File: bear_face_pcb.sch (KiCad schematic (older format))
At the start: 201 parts, among them J1 GT-USB-7010EN, J2 Conn_02x03_Odd_Even, SW1 RESET, U1 ATmega32U4-AU, U2 SRV05-4, Y1 16MHz

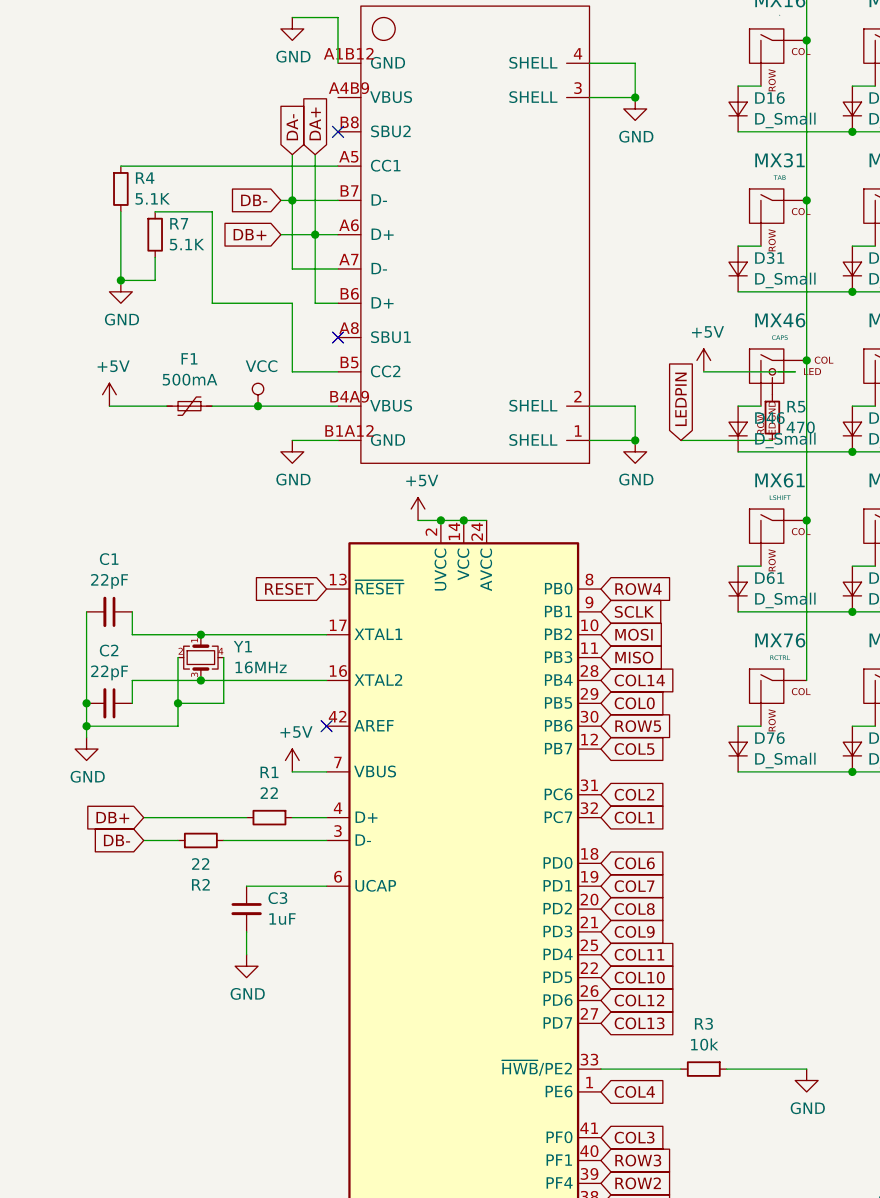
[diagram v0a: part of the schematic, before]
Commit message: renumbered pulldown resistors
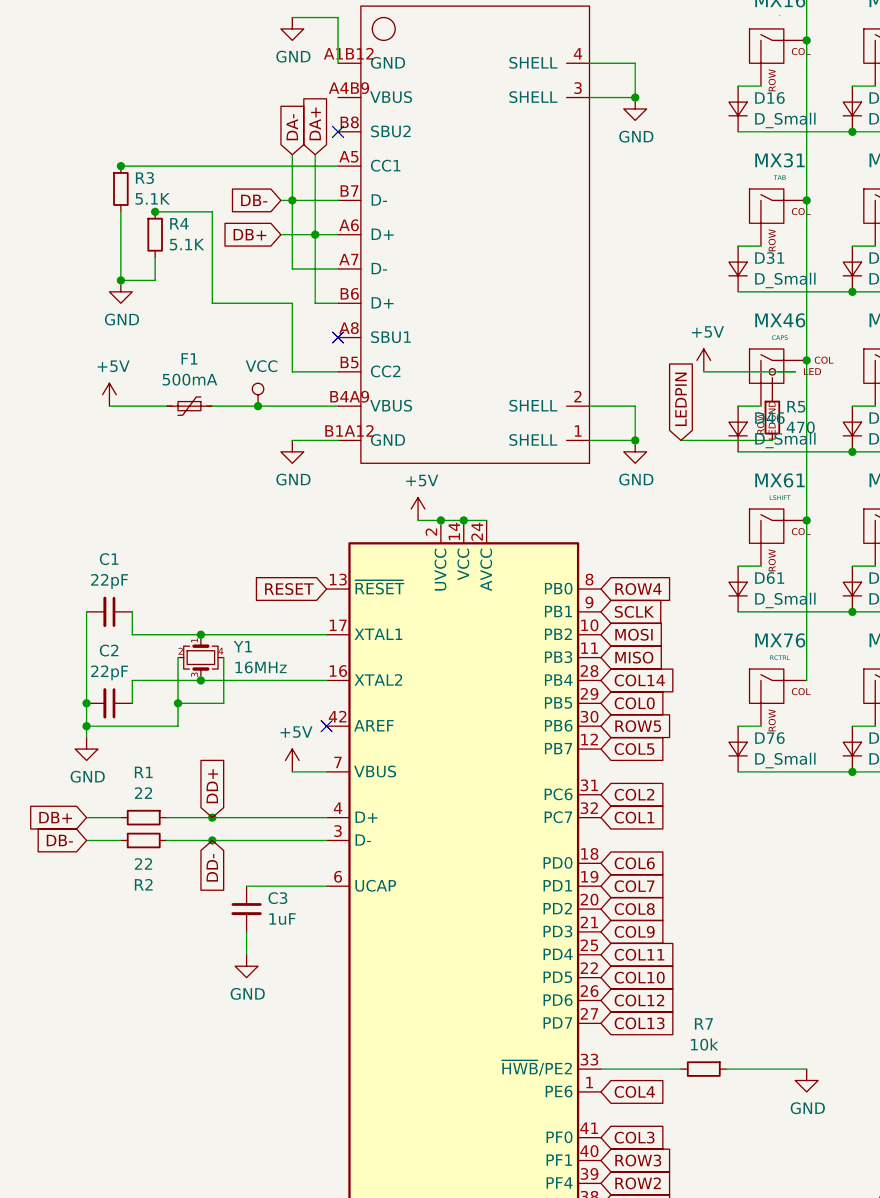
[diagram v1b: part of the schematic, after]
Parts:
- renumbered R4 to R3, R7 to R4, R3 to R7
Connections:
- net DD-: now reaches R2.2, U1.3 (D-)
- net DD+: now reaches R1.1, U1.4 (D+)
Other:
- moved on the sheet: R1, R2
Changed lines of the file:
@@
 	8500 5550 8500 5650
 $Comp
-L Device:R_Small R3
+L Device:R_Small R7
 U 1 1 5E285AAF
 P 3400 6250
-F 0 "R3" V 3204 6250 50  0000 C CNN
+F 0 "R7" V 3204 6250 50  0000 C CNN
 F 1 "10k" V 3295 6250 50  0000 C CNN
 F 2 "Resistor_SMD:R_0805_2012Metric" H 3400 6250 50  0001 C CNN
@@
 Text GLabel 5500 5900 2    50   Input ~ 0
 DA+
-Text GLabel 1550 2450 0    50   Input ~ 0
-DB-
 Text GLabel 3300 3500 1    50   Input ~ 0
 LEDPIN
-Text GLabel 950  5150 0    50   Input ~ 0
-DB+
-Text GLabel 950  5250 0    50   Input ~ 0
-DB-
 Wire Wire Line
 	2250 7450 2350 7450
@@
 Wire Wire Line
 	1700 2600 1550 2600
-Text GLabel 1550 2600 0    50   Input ~ 0
-DB+
 Wire Wire Line
 	1700 2250 1700 2600
@@
 	1600 2450 1550 2450
 $Comp
-L Device:R_Small R4
+L Device:R_Small R3
 U 1 1 65B37F14
 P 850 2400
-F 0 "R4" H 909 2446 50  0000 L CNN
+F 0 "R3" H 909 2446 50  0000 L CNN
 F 1 "5.1K" H 909 2355 50  0000 L CNN
 F 2 "Resistor_SMD:R_0805_2012Metric" H 850 2400 50  0001 C CNN
@@
 	1250 2500 1000 2500
 $Comp
-L Device:R_Small R7
+L Device:R_Small R4
 U 1 1 65B89020
 P 1000 2600
-F 0 "R7" H 1059 2646 50  0000 L CNN
+F 0 "R4" H 1059 2646 50  0000 L CNN
 F 1 "5.1K" H 1059 2555 50  0000 L CNN
 F 2 "Resistor_SMD:R_0805_2012Metric" H 1000 2600 50  0001 C CNN
@@
 L Device:R_Small R1
 U 1 1 66036275
-P 1500 5150
-F 0 "R1" V 1304 5150 50  0000 C CNN
-F 1 "22" V 1395 5150 50  0000 C CNN
-F 2 "Resistor_SMD:R_0805_2012Metric" H 1500 5150 50  0001 C CNN
-F 3 "~" H 1500 5150 50  0001 C CNN
-	1    1500 5150
+P 950 5150
+F 0 "R1" V 754 5150 50  0000 C CNN
+F 1 "22" V 845 5150 50  0000 C CNN
+F 2 "Resistor_SMD:R_0805_2012Metric" H 950 5150 50  0001 C CNN
+F 3 "~" H 950 5150 50  0001 C CNN
+	1    950  5150
 	0    1    1    0
 $EndComp
-Wire Wire Line
-	1750 5150 1600 5150
-Wire Wire Line
-	1400 5150 950  5150
-Wire Wire Line
-	1100 5250 950  5250
-Wire Wire Line
-	1300 5250 1750 5250
 $Comp
 L Device:R_Small R2
 U 1 1 66037A5E
-P 1200 5250
-F 0 "R2" V 1004 5250 50  0000 C CNN
-F 1 "22" V 1095 5250 50  0000 C CNN
-F 2 "Resistor_SMD:R_0805_2012Metric" H 1200 5250 50  0001 C CNN
-F 3 "~" H 1200 5250 50  0001 C CNN
-	1    1200 5250
+P 950 5250
+F 0 "R2" V 754 5250 50  0000 C CNN
+F 1 "22" V 845 5250 50  0000 C CNN
+F 2 "Resistor_SMD:R_0805_2012Metric" H 950 5250 50  0001 C CNN
+F 3 "~" H 950 5250 50  0001 C CNN
+	1    950  5250
 	0    -1   -1   0
 $EndComp
+Text GLabel 700  5250 0    50   Input ~ 0
+DB-
+Text GLabel 700  5150 0    50   Input ~ 0
+DB+
+Text GLabel 1550 2600 0    50   Input ~ 0
+DB+
+Text GLabel 1550 2450 0    50   Input ~ 0
+DB-
+Text GLabel 1250 5150 1    50   Input ~ 0
+DD+
+Wire Wire Line
+	700  5150 850  5150
+Wire Wire Line
+	1050 5150 1250 5150
+Wire Wire Line
+	700  5250 850  5250
+Wire Wire Line
+	1050 5250 1250 5250
+Connection ~ 1250 5150
+Wire Wire Line
+	1250 5150 1750 5150
+Connection ~ 1250 5250
+Wire Wire Line
+	1250 5250 1750 5250
+Text GLabel 1250 5250 3    50   Input ~ 0
+DD-
+Connection ~ 850  2300
+Connection ~ 1000 2500
 $EndSCHEMATC

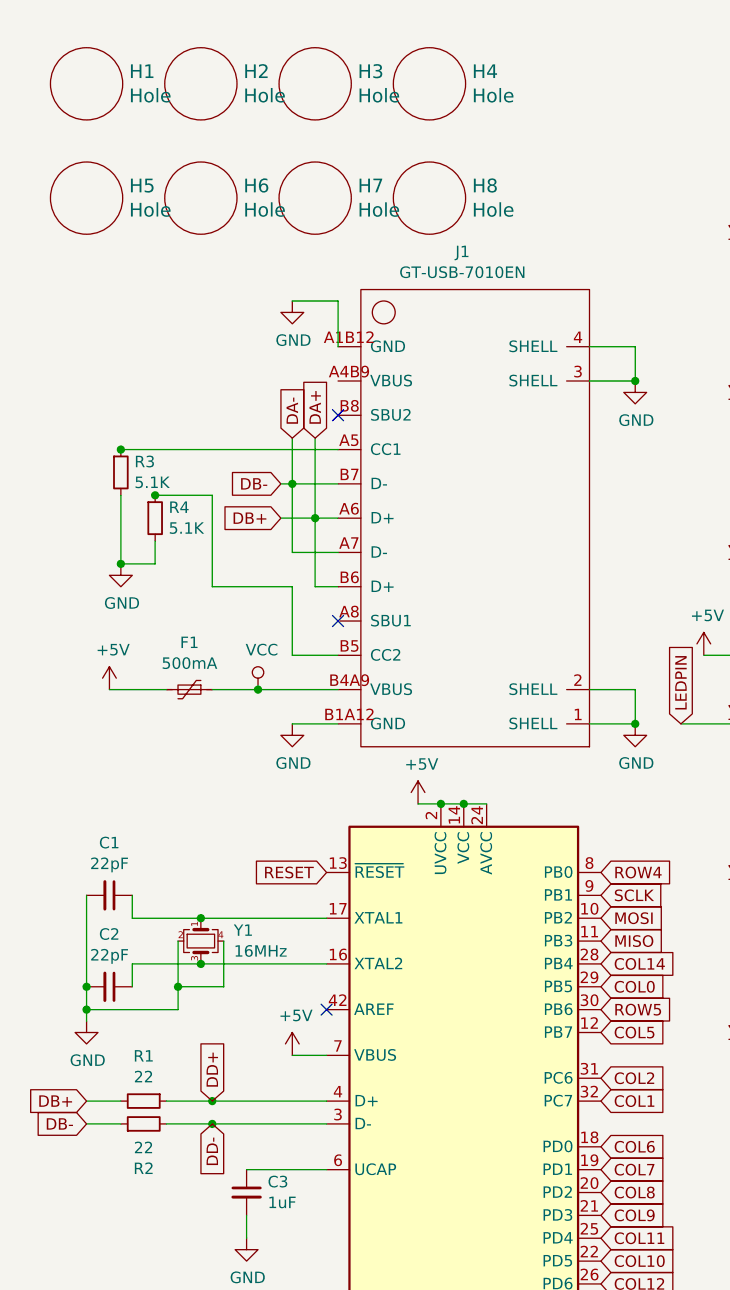
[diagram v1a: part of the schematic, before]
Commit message: numbering tweaks, grounded pcb to plate hole, silks edit
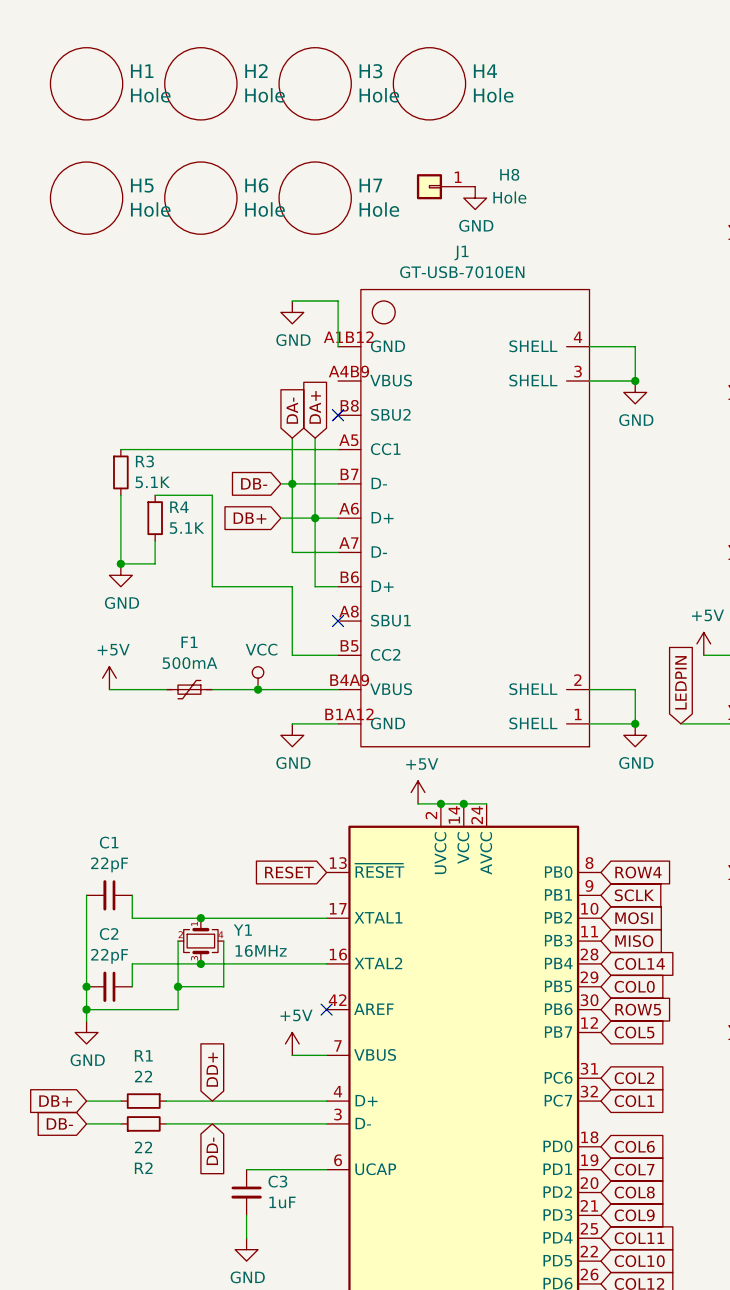
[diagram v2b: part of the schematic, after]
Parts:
- removed H8: Hole, bear_face_parts:MountingHole_3mm, symbol keebio:Hole
- added H8: Hole, bear_face_parts:MountingHole_3mm, symbol Connector_Generic:Conn_01x01
- J1: LCSC# (none) -> C3001297
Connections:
- net GND: now also H8.1 (Pin_1)
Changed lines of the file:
@@
-$EndComp
-$Comp
-L keebio:Hole H8
-U 1 1 5E160711
-P 2200 1200
-F 0 "H8" H 2386 1253 60  0000 L CNN
-F 1 "Hole" H 2386 1147 60  0000 L CNN
-F 2 "bear_face_parts:MountingHole_3mm" H 2200 1200 60  0001 C CNN
-F 3 "" H 2200 1200 60  0001 C CNN
-	1    2200 1200
-	1    0    0    -1
 $EndComp
 $Comp
@@
 F 2 "bear_face_parts:USB-C-SMD_G-SWITCH_GT-USB-7010EN" H 2400 2500 50  0001 C CNN
 F 3 "" H 2400 2500 50  0001 C CNN
+F 4 "C3001297" H 2400 2600 50  0001 C CNN "LCSC#"
 	1    2400 2600
 	1    0    0    -1
@@
 F 2 "Resistor_SMD:R_0805_2012Metric" H 850 2400 50  0001 C CNN
 F 3 "~" H 850 2400 50  0001 C CNN
+F 4 "" H 850 2400 50  0001 C CNN "LCSC#"
 	1    850  2400
 	1    0    0    -1
@@
 F 2 "Resistor_SMD:R_0805_2012Metric" H 1000 2600 50  0001 C CNN
 F 3 "~" H 1000 2600 50  0001 C CNN
+F 4 "" H 1000 2600 50  0001 C CNN "LCSC#"
 	1    1000 2600
 	1    0    0    -1
@@
 	700  5150 850  5150
 Wire Wire Line
-	1050 5150 1250 5150
-Wire Wire Line
 	700  5250 850  5250
-Wire Wire Line
-	1050 5250 1250 5250
-Connection ~ 1250 5150
-Wire Wire Line
-	1250 5150 1750 5150
-Connection ~ 1250 5250
-Wire Wire Line
-	1250 5250 1750 5250
 Text GLabel 1250 5250 3    50   Input ~ 0
 DD-
-Connection ~ 850  2300
-Connection ~ 1000 2500
+Wire Wire Line
+	1050 5150 1750 5150
+Wire Wire Line
+	1050 5250 1750 5250
+$Comp
+L Connector_Generic:Conn_01x01 H8
+U 1 1 664A148D
+P 2200 1150
+F 0 "H8" H 1850 1100 50  0000 C CNN
+F 1 "Hole" H 1850 1200 50  0000 C CNN
+F 2 "bear_face_parts:MountingHole_3mm" H 2200 1150 50  0001 C CNN
+F 3 "~" H 2200 1150 50  0001 C CNN
+	1    2200 1150
+	-1   0    0    1
+$EndComp
+$Comp
+L power:GND #PWR0111
+U 1 1 664D0BC7
+P 2400 1150
+F 0 "#PWR0111" H 2400 900 50  0001 C CNN
+F 1 "GND" H 2405 977 50  0000 C CNN
+F 2 "" H 2400 1150 50  0001 C CNN
+F 3 "" H 2400 1150 50  0001 C CNN
+	1    2400 1150
+	1    0    0    -1
+$EndComp
 $EndSCHEMATC

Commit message: ready for JLC, routing/place tweaks
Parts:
- C1, C2: LCSC (none) -> C1804; LCSC# C1804 -> (none)
- C3: LCSC (none) -> C28323; LCSC# C28323 -> (none)
- C4, C5, C6: LCSC (none) -> C49678; LCSC# C49678 -> (none)
- C7: LCSC (none) -> C15850; LCSC# C15850 -> (none)
- D1, D10, D11, D12, D13, D14, D15, D16, D17, D18, D19, D2, D20, D21, D22, D23, D24, D25, D26, D27, D28, D29, D3, D30, D31, D32, D33, D34, D35, D36, D37, D38, D39, D4, D40, D41, D42, D43, D44, D45, D46, D47, D48, D49, D5, D50, D51, D52, D53, D54, D55, D56, D57, D58, D59, D6, D60, D61, D62, D63, D64, D65, D66, D67, D68, D69, D7, D70, D71, D72, D73, D74, D75, D76, D77, D78, D79, D8, D80, D81, D82, D83, D84, D85, D9: LCSC (none) -> C81598; LCSC# C81598 -> (none)
- F1: LCSC (none) -> C70076; LCSC# C70076 -> (none)
- J1: LCSC (none) -> C3001297; LCSC# C3001297 -> (none)
- R1, R2: LCSC (none) -> C17561
- R3, R4: value 5.1K -> 5.1k; LCSC (none) -> C2907269
- R5: LCSC (none) -> C17710; LCSC# C17710 -> (none)
- R6, R7: LCSC (none) -> C17414; LCSC# C17414 -> (none)
- U1: LCSC (none) -> C44854; LCSC# C44854 -> (none)
- U2: LCSC (none) -> C85364; LCSC# C85364 -> (none)
- Y1: LCSC (none) -> C13738; LCSC# C13738 -> (none)
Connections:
- net VCC: now also J1.A4B9 (VBUS)
- net DD+ renamed D+
- net DD- renamed D-
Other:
- moved on the sheet: F1

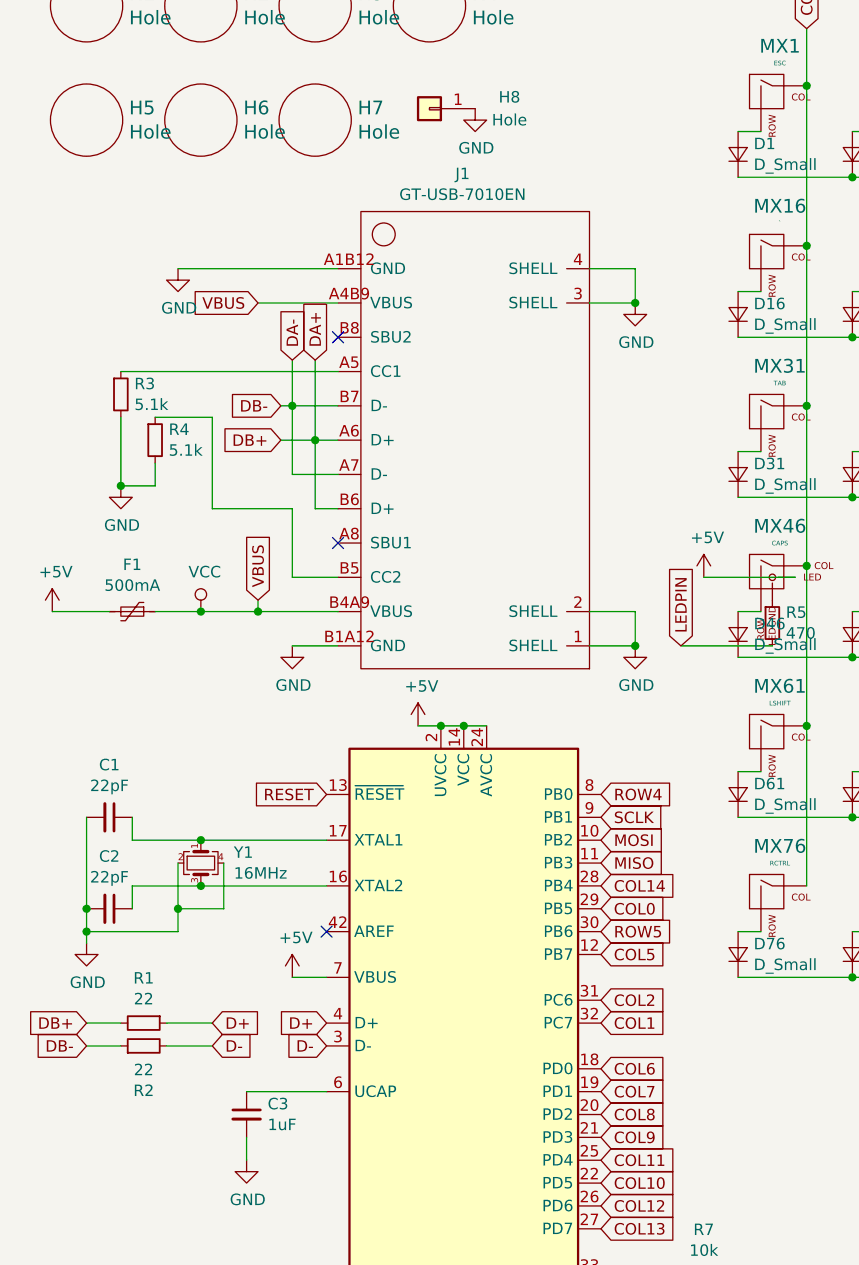
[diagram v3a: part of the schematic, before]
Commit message: changed usb to 31_M12, minor silk tweaks, fixed BOM/CPL
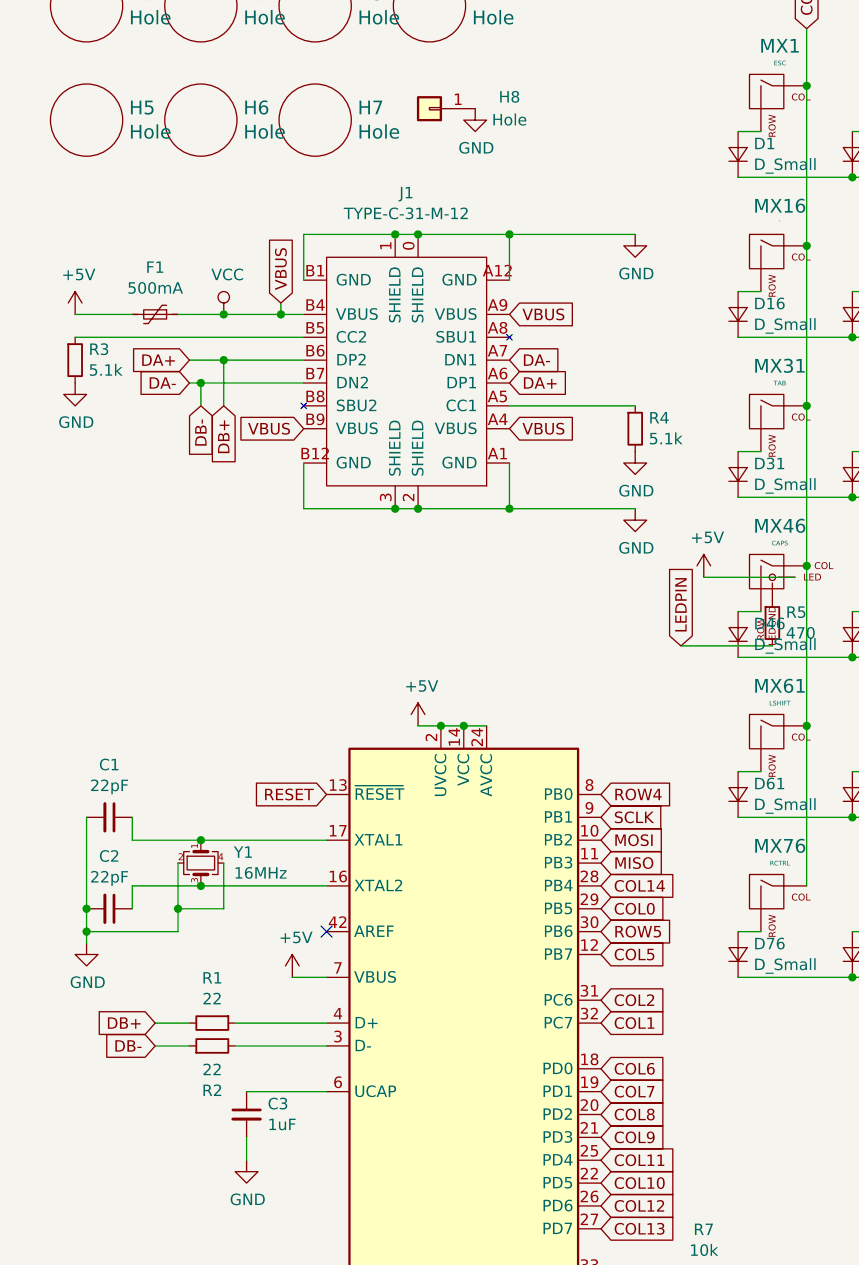
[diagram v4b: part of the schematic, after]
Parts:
- removed J1: GT-USB-7010EN, bear_face_parts:USB-C-SMD_G-SWITCH_GT-USB-7010EN, symbol bear_face_pcb:GT-USB-7010EN
- added J1: TYPE-C-31-M-12, bear_face_parts:USB-C_SMD-TYPE-C-31-M-12, symbol bear_face_pcb:TYPE-C-31-M-12
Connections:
- net DA+: now also J1.A6 (DP1), J1.B6 (DP2)
- net DA-: now also J1.A7 (DN1), J1.B7 (DN2)
- net GND: now also J1.0 (SHIELD), J1.1 (SHIELD), J1.2 (SHIELD), J1.3 (SHIELD), J1.A1 (GND), J1.A12 (GND), J1.B1 (GND), J1.B12 (GND)
- net VCC: now also J1.A4 (VBUS), J1.A9 (VBUS), J1.B4 (VBUS), J1.B9 (VBUS)
- net at R3.1: now also J1.B5 (CC2)
- net at R4.1: now also J1.A5 (CC1)
- net D+: no longer names the net of R1.1, U1.4 (D+)
- net D-: no longer names the net of R2.2, U1.3 (D-)
- no-connect marks 5 -> 3
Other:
- moved on the sheet: F1, R1, R2, R3, R4
